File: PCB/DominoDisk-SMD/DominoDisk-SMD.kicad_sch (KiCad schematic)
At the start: 30 parts, among them J1 Daisy port out, J2 ICSP_ISP6, J3 UART, J4 Daisy port in, K1 HYC77-TF09-200, U1 PC817C-S, U2 ATmega328P-AU, U3 SE5218, U4 TXB0104QPWRQ1, Y1 16MHz

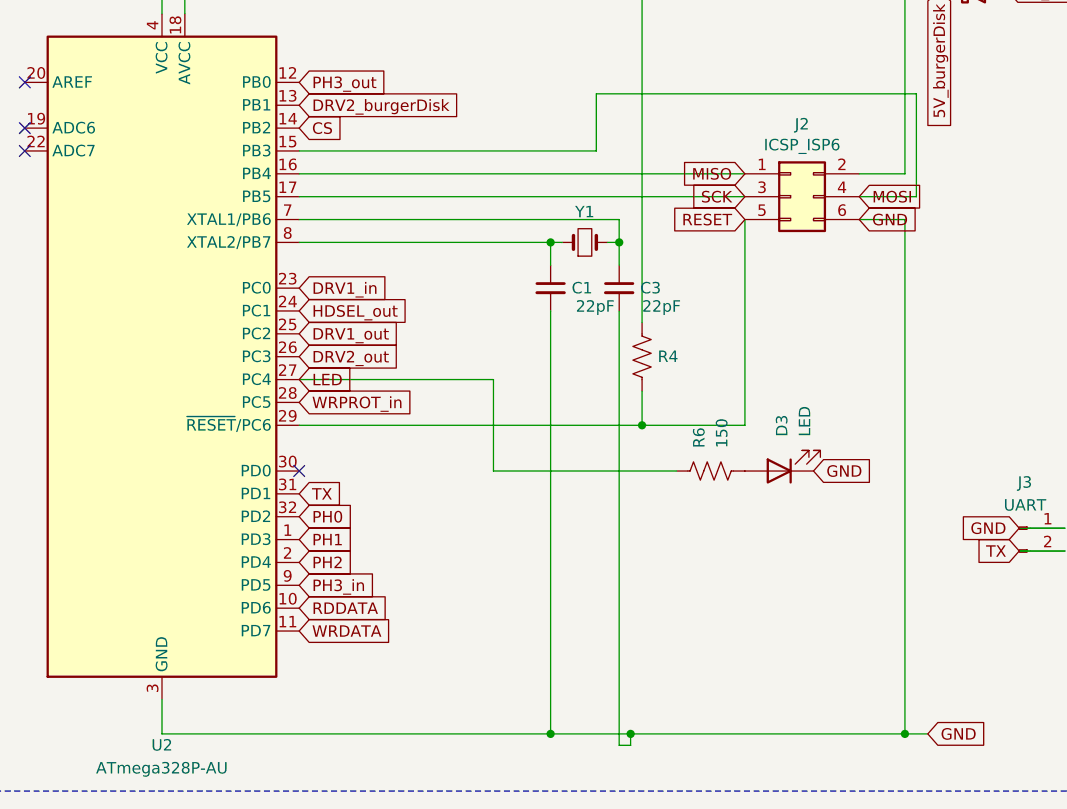
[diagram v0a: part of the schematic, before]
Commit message: Renames, move to resonator on Domino
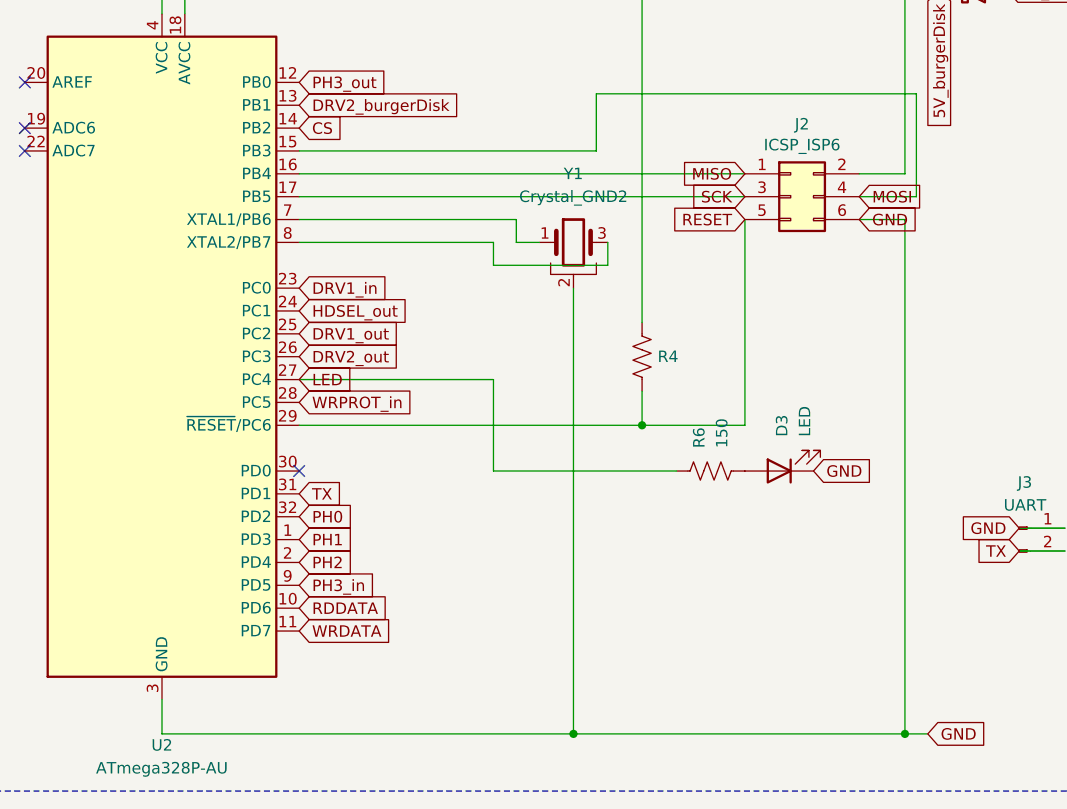
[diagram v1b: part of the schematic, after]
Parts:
- removed C1, C3: 22pF, Capacitor_SMD:C_0603_1608Metric, symbol Device:C_Small
- removed Y1: 16MHz, Crystal:Crystal_SMD_HC49-SD, symbol Device:Crystal_Small
- added Y1: Crystal_GND2, Crystal:Resonator_SMD_Murata_CSTxExxV-3Pin_3.0x1.1mm, symbol Device:Crystal_GND2
- D1: footprint Diode_SMD:D_SOD-323 -> Diode_SMD:D_SOD-123F; LCSC C5240366 -> C51315007
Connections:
- net GND: now also Y1.2
- net at U2.8 (XTAL2/PB7): now also Y1.3
- net at U2.7 (XTAL1/PB6): now also Y1.1
